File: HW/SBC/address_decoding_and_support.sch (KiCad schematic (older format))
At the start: 9 parts, among them Q1 DS1813, SW1 RESET, U7 ispMACH4A5, U8 74HC74, X1 8 MHz

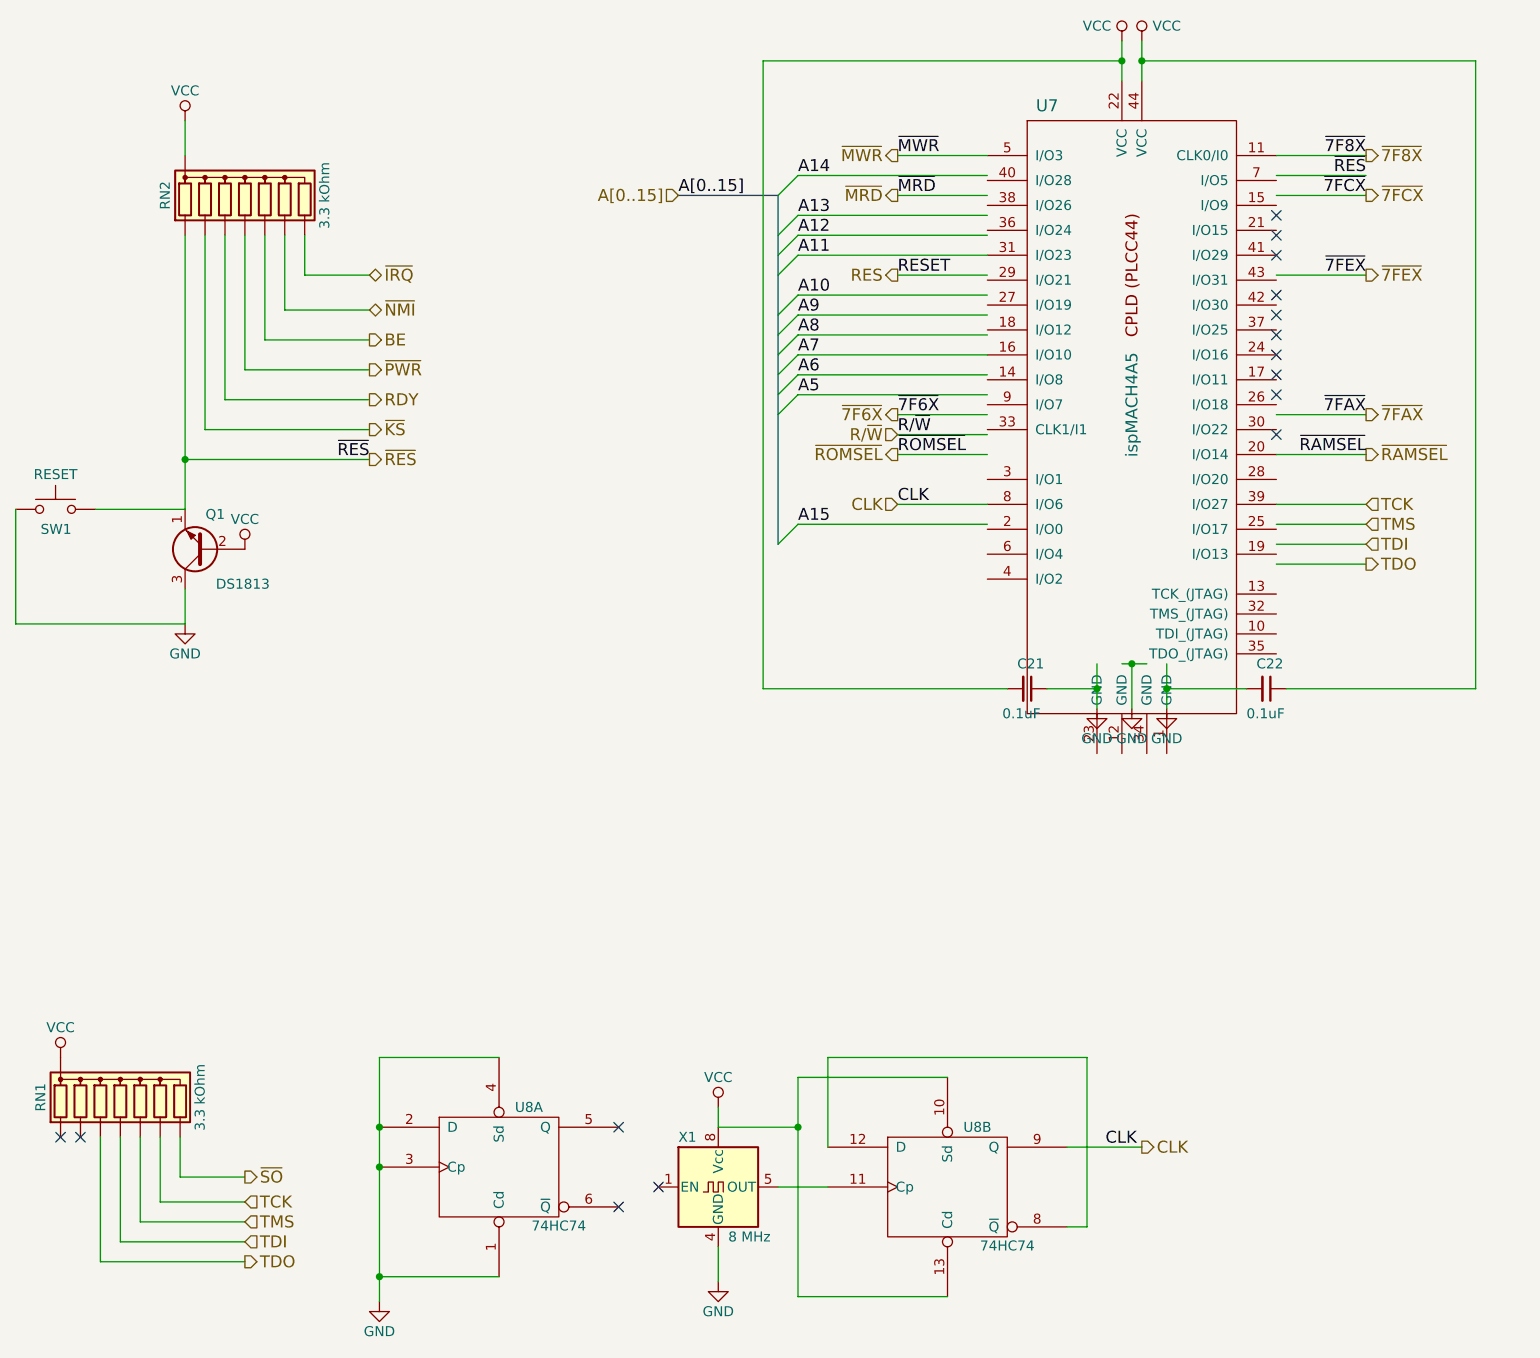
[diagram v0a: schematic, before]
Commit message: Added CPLD to schematics. Updates rest of schematics to use CPLD
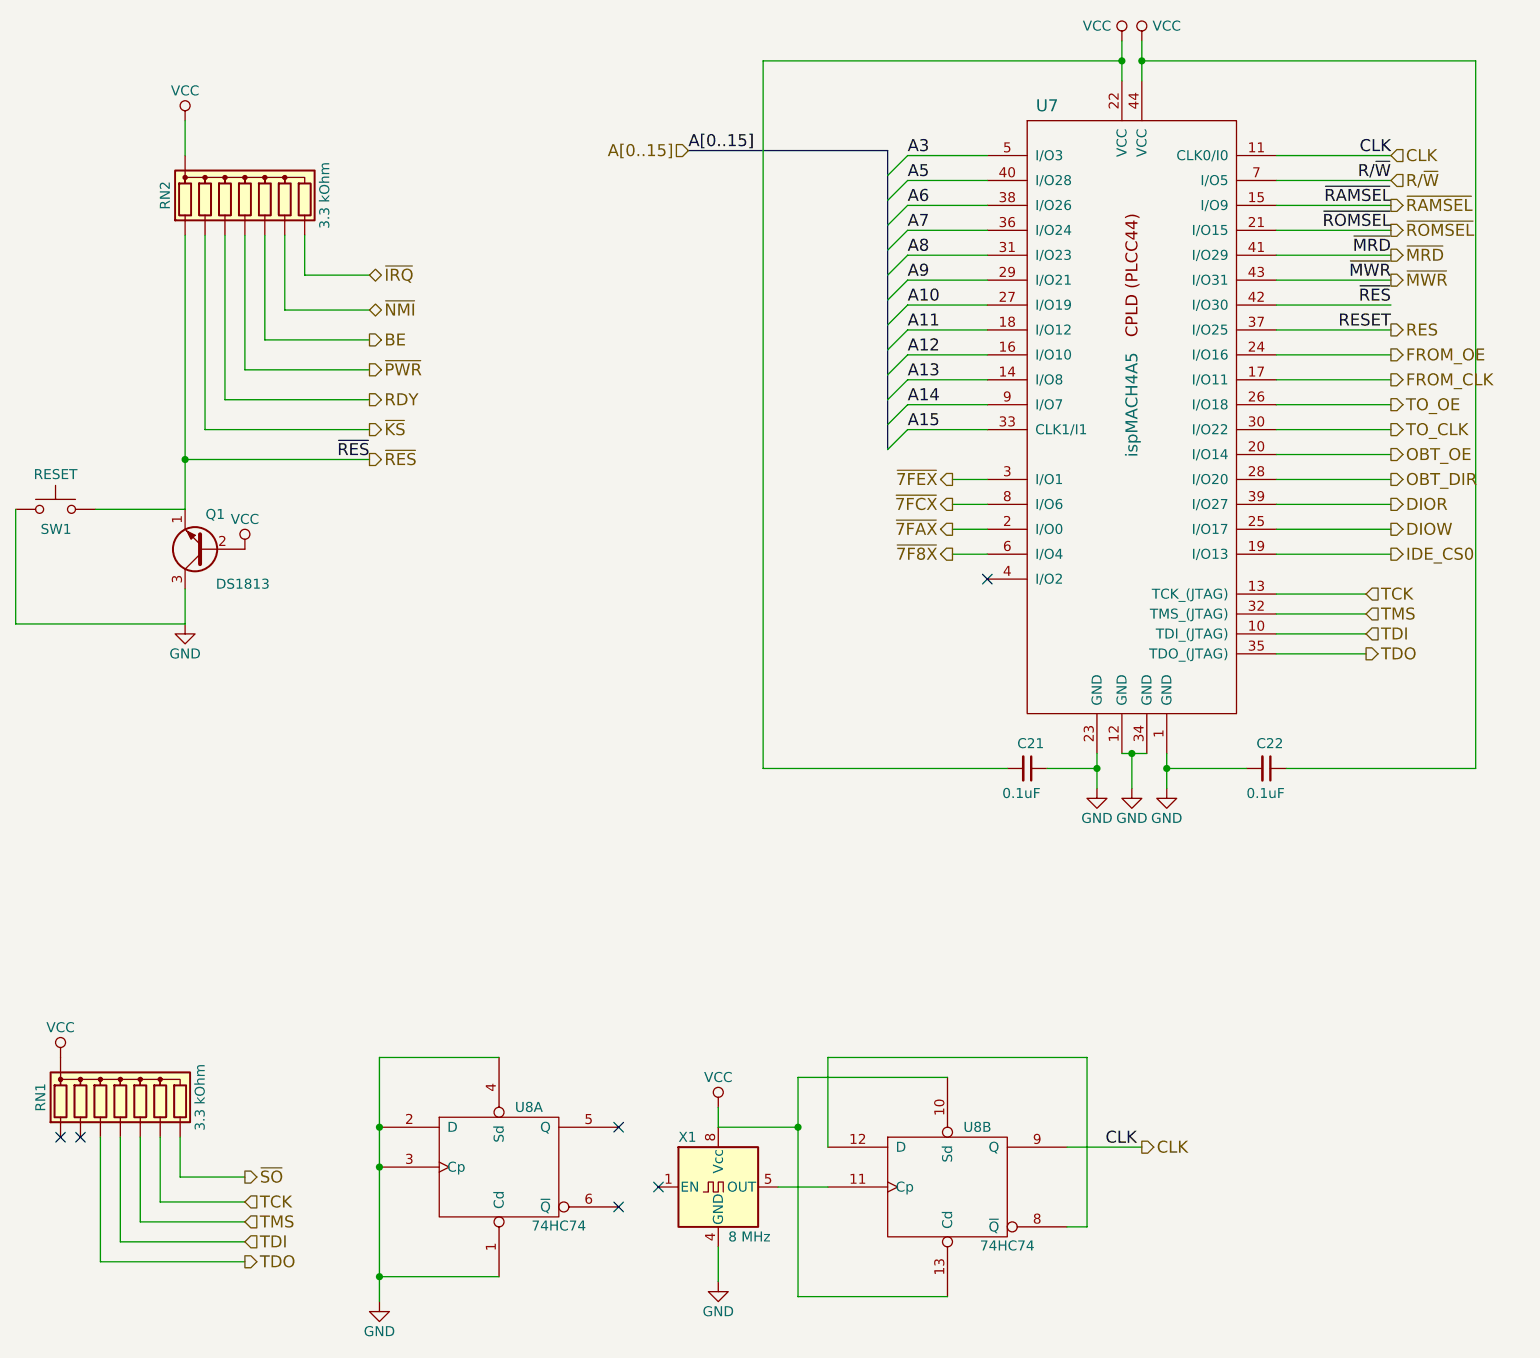
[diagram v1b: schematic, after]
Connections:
- net labels added: A3, DIOR, DIOW, FROM_CLK, FROM_OE, IDE_CS0, OBT_DIR, OBT_OE, TO_CLK, TO_OE
- net labels removed: ~7F6X
- wire segments 86 -> 95
- no-connect marks 15 -> 6
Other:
- moved on the sheet: C21, C22
